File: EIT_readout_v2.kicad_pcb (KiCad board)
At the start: 2 copper layers, 103.9 x 63.3 mm, 16 parts, among them J4 Conn_Coaxial_Small, J5 Conn_Coaxial_Small, J6 Conn_Coaxial_Small, U1 Teensy4.0, U2 MAX336CWI+, U3 MAX336CWI+, U4 LTC1983ES6-3-TRPBF

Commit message: added M3 Mounting holes to the PCB
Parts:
- added REF**: MountingHole_3.2mm_M3, MountingHole:MountingHole_3.2mm_M3, F.Cu at (175.3, 52.1)
- added REF**: MountingHole_3.2mm_M3, MountingHole:MountingHole_3.2mm_M3, F.Cu at (92.7, 52.1)
- added REF**: MountingHole_3.2mm_M3, MountingHole:MountingHole_3.2mm_M3, F.Cu at (92.7, 100.3)

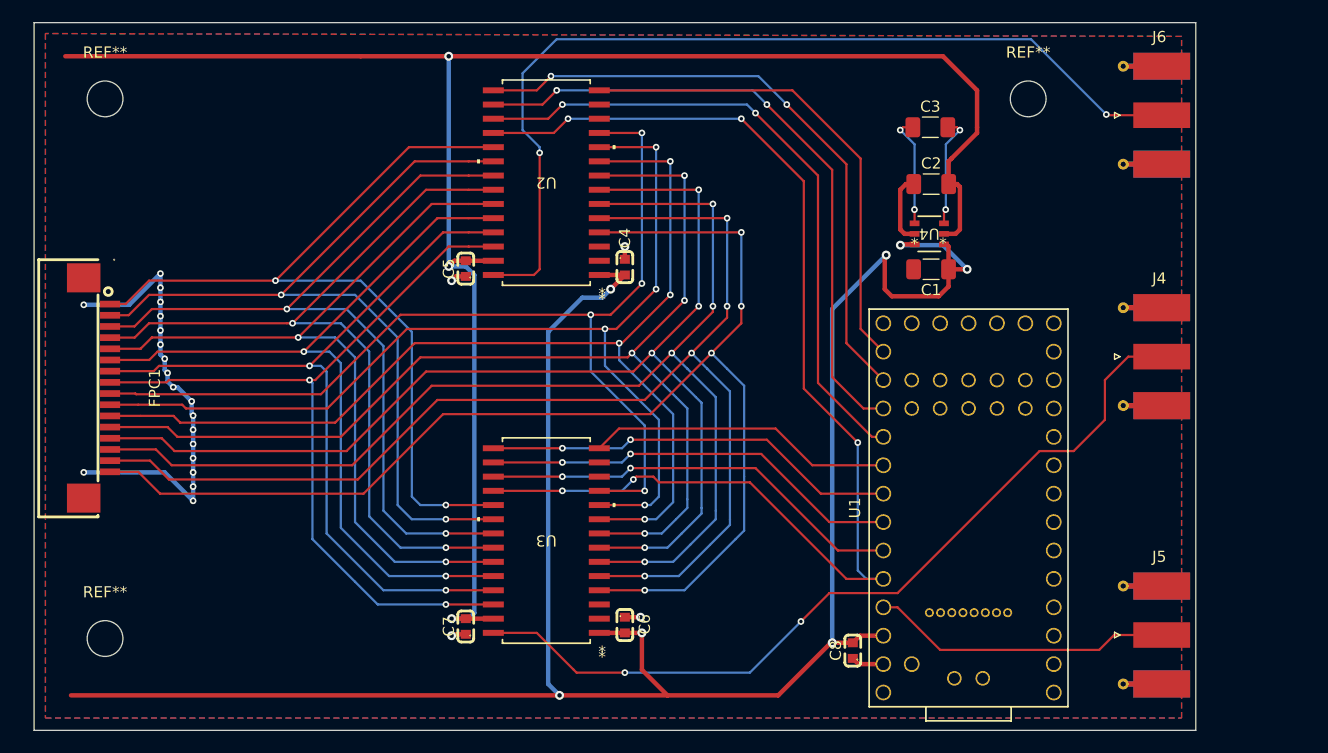
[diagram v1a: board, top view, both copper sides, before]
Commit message: Added via to ground plane, also added footprint for MAX336 to library
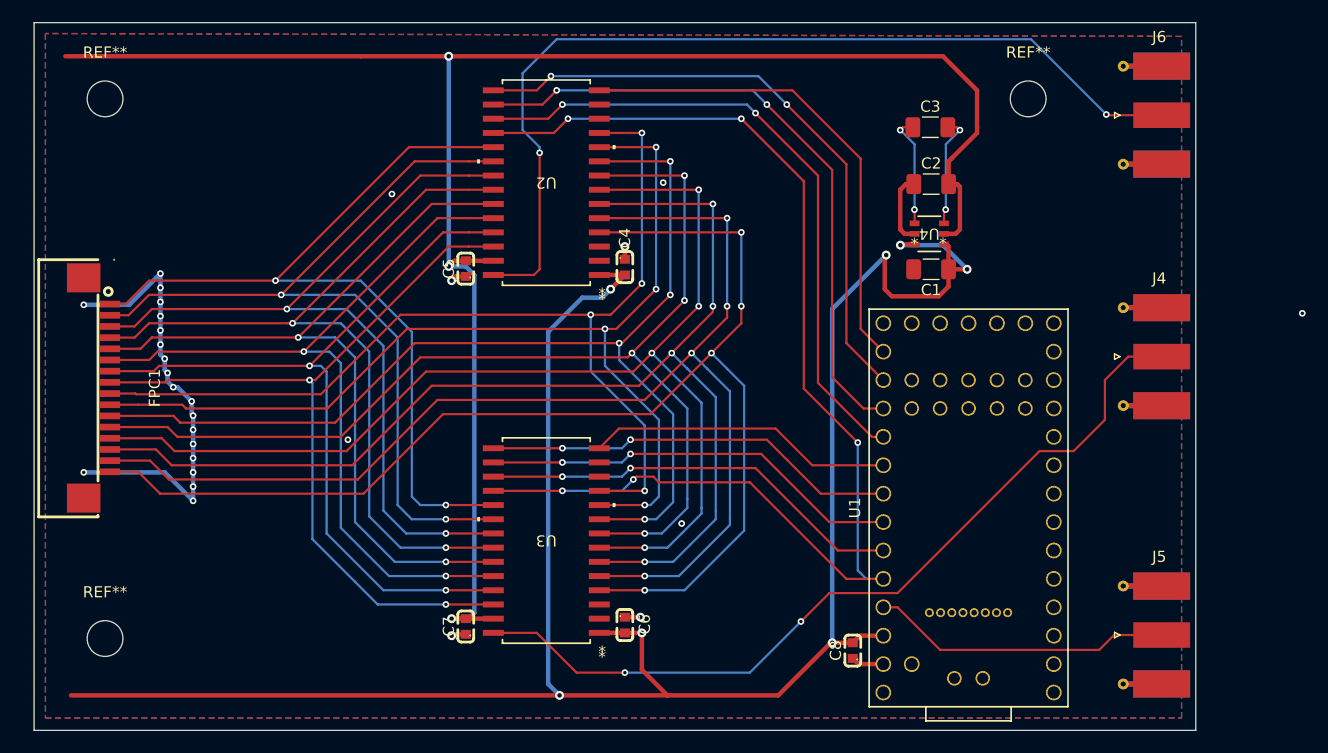
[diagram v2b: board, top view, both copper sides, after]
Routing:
- net GND: vias 23 -> 27
- net (no net): vias 0 -> 1
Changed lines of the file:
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@@
 			(outputformat 1)
 			(mirror no)
-			(drillshape 1)
+			(drillshape 0)
 			(scaleselection 1)
-			(outputdirectory "")
+			(outputdirectory "./")
 		)
 	)
@@
 		(layer "Edge.Cuts")
 	)
+	(via
+		(at 199.771 71.247)
+		(size 0.6)
+		(drill 0.3)
+		(layers "F.Cu" "B.Cu")
+		(net 0)
+	)
 	(segment
 		(start 132.334 53.848)
@@
 	)
 	(via
+		(at 114.427 82.55)
+		(size 0.6)
+		(drill 0.3)
+		(layers "F.Cu" "B.Cu")
+		(free yes)
+		(net 68)
+	)
+	(via
 		(at 97.663 74.041)
 		(size 0.6)
@@
 	)
 	(via
+		(at 118.364 60.579)
+		(size 0.6)
+		(drill 0.3)
+		(layers "F.Cu" "B.Cu")
+		(free yes)
+		(net 68)
+	)
+	(via
 		(at 98.044 75.311)
 		(size 0.6)
@@
 	)
 	(via
+		(at 142.621 59.563)
+		(size 0.6)
+		(drill 0.3)
+		(layers "F.Cu" "B.Cu")
+		(free yes)
+		(net 68)
+	)
+	(via
 		(at 97.663 68.961)
 		(size 0.6)
@@
 		(size 0.6)
 		(drill 0.3)
+		(layers "F.Cu" "B.Cu")
+		(free yes)
+		(net 68)
+	)
+	(via
+		(at 144.272 90.043)
+		(size 0.6)
+		(drill 0.3)

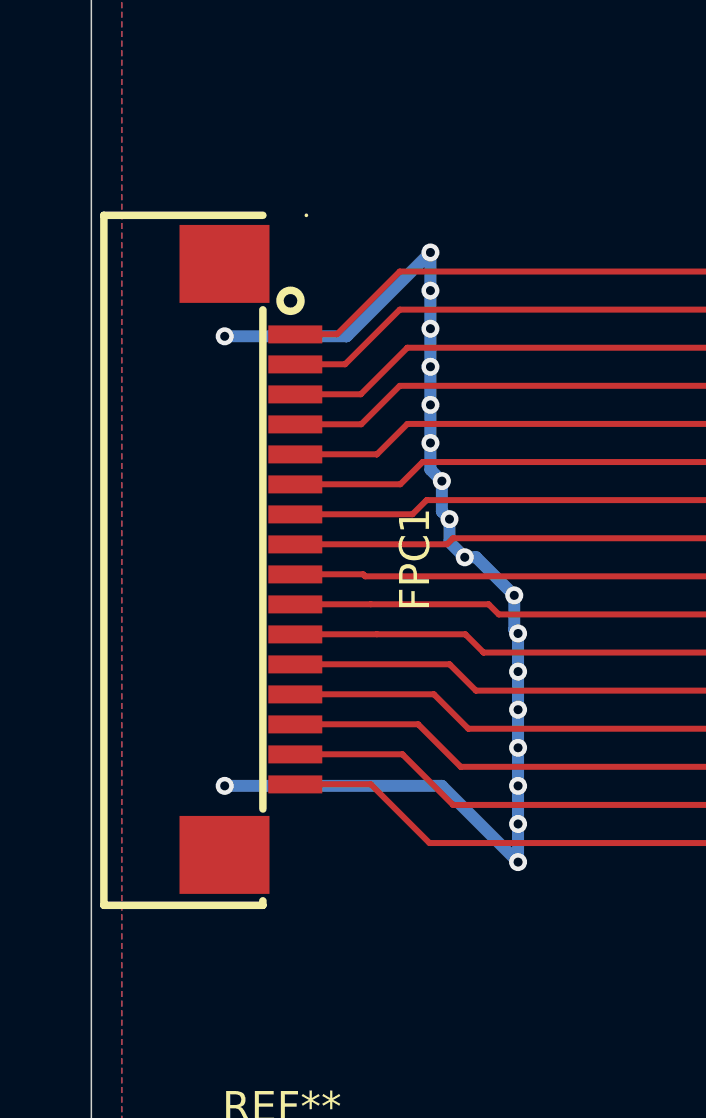
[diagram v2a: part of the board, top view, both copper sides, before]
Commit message: changed the readout PCB FPC holder to 18 pins to accommodate ground
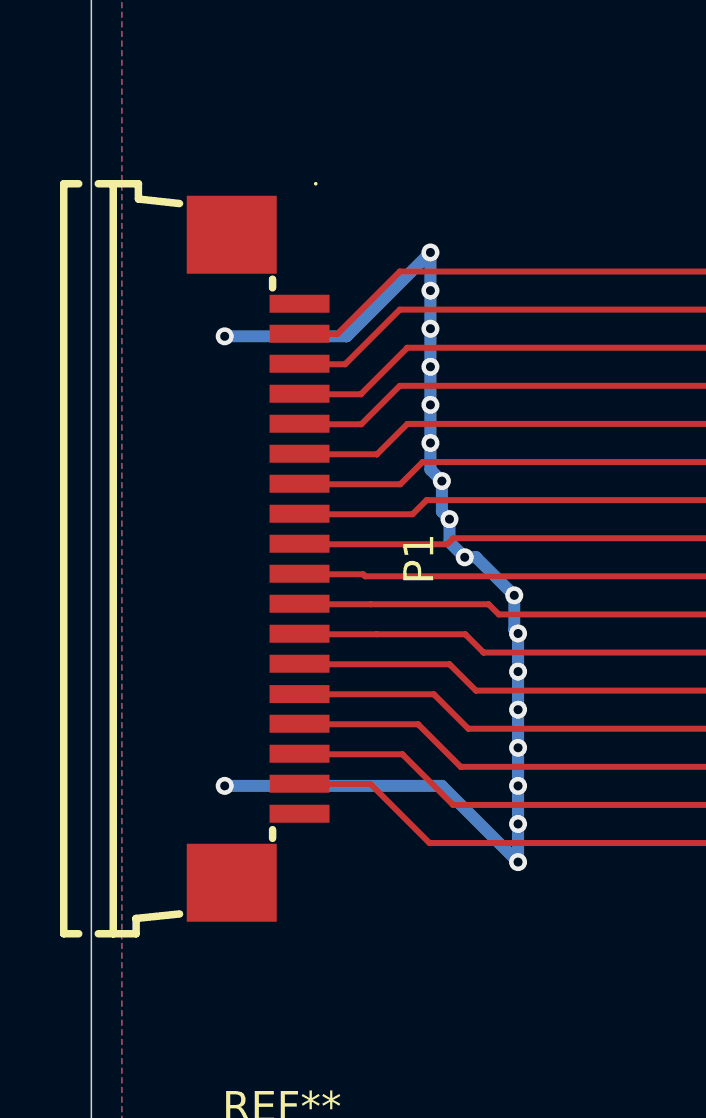
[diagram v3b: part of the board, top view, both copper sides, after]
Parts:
- removed FPC1: AFA07-S16FCC-00, easyeda2kicad:FPC-SMD_16P-P1.00_AFA07-S16FCC-00
- added P1: FPCConnector18PUnder the next 1mm, easyeda2kicad:FPC-SMD_18P-P1.00_AFA07-S18FCC-00, F.Cu at (92.2, 77.9)
